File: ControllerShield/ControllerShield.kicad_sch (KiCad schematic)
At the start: 25 parts, among them J1 Power, J2 Digital/PWM, J3 Analog, J4 Digital/PWM, J5 Conn_02x05_Odd_Even, J6 Debug Point, SW1 Small Switch TH, U1 COM-09032, U2 LIS3DHTR, U3 TLV75533PDBV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

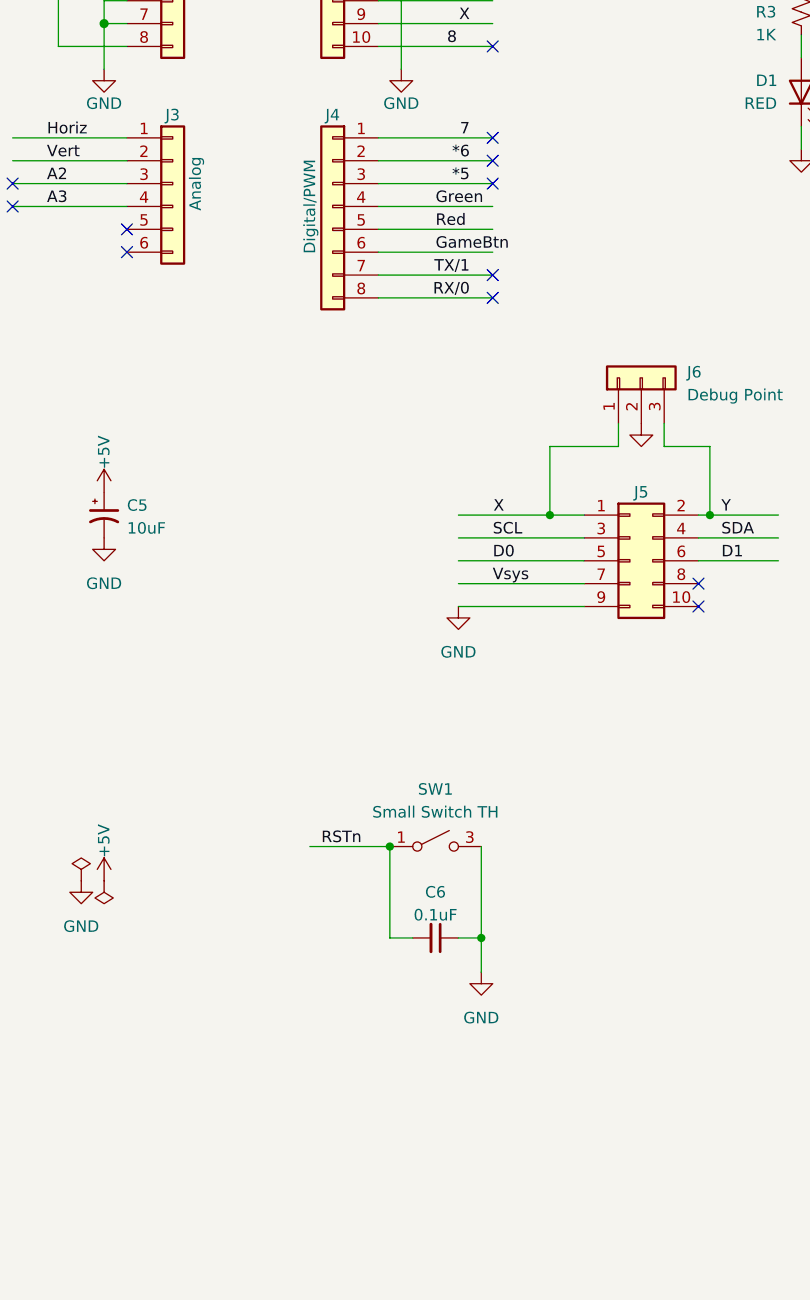
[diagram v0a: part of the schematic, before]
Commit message: Add a second switch to the controller board.
Generate V0.9 gerbers with QRCode.
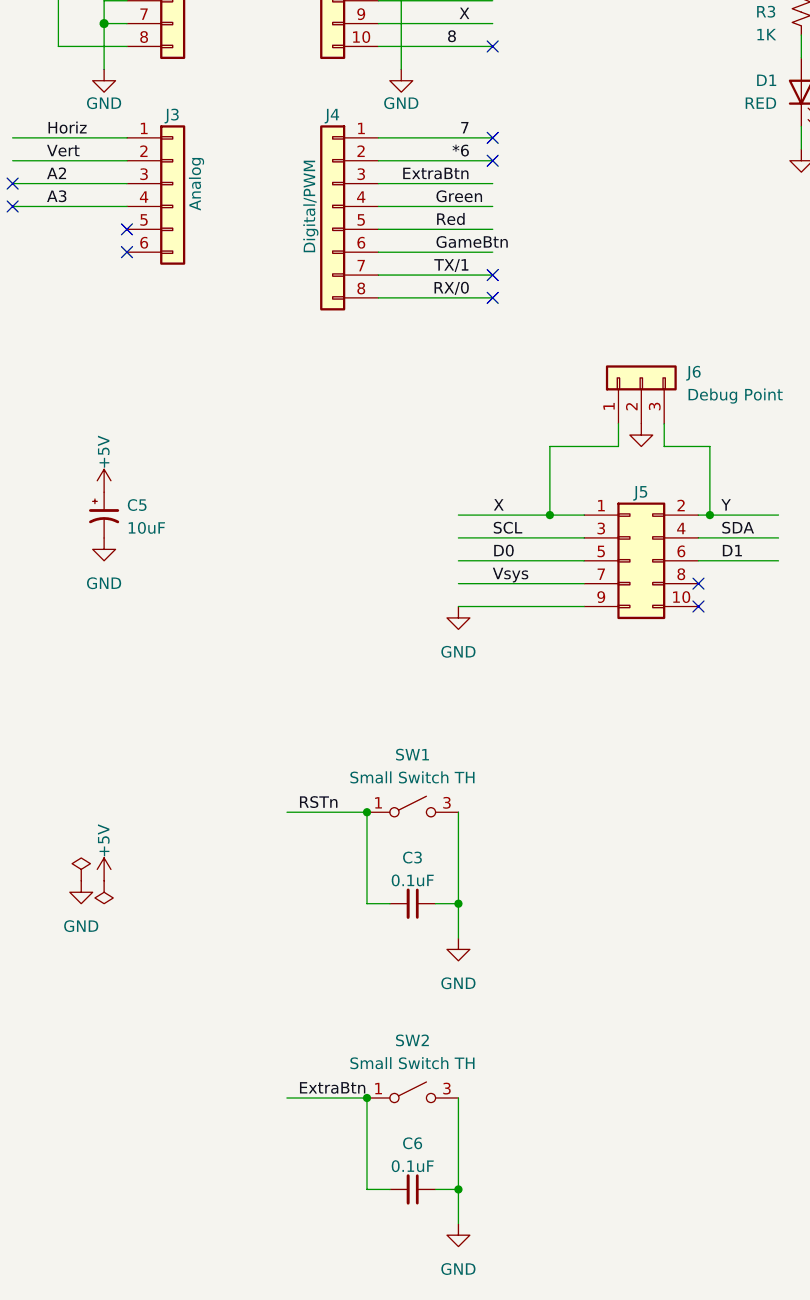
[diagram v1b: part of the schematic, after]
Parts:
- added C3: 0.1uF, Capacitor_SMD:C_0603_1608Metric, symbol Device:C_Small
- added SW2: Small Switch TH, Footprints:SW4_1825910-B_TEC, symbol Local:Small Switch TH
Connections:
- net GND: now also C3.1, SW2.3 (B), SW2.4 (B)
- net RSTn: now also C3.2; no longer C6.2
- net *5 renamed ExtraBtn
- net ExtraBtn: now also C6.2, SW2.1 (A), SW2.2 (A)
- no-connect marks 22 -> 21

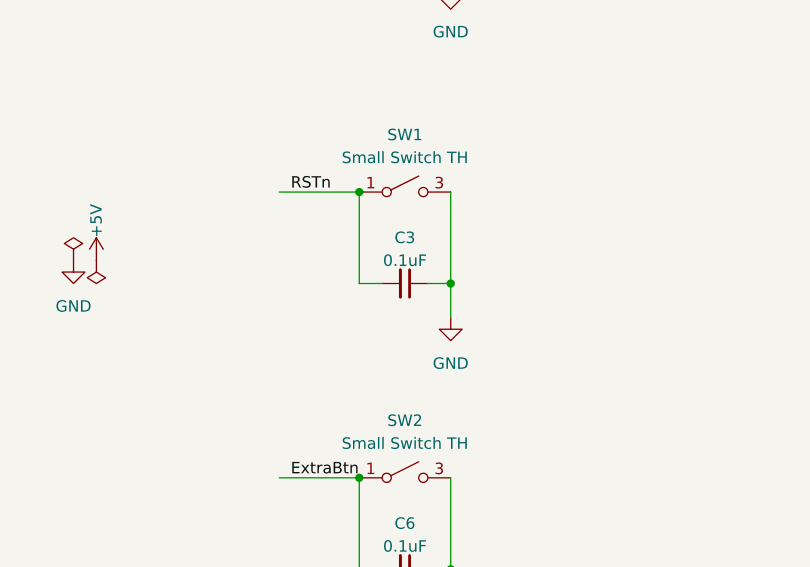
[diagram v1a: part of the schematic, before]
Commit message: add vendor id for level shifter
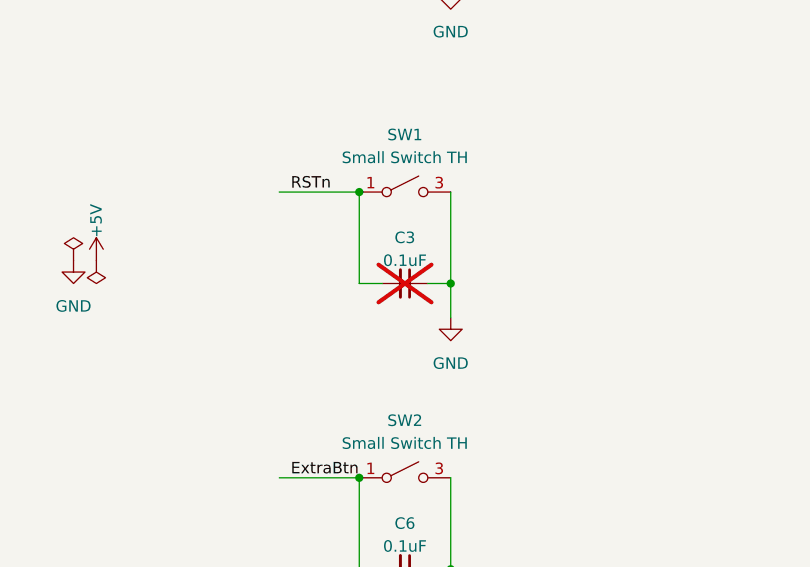
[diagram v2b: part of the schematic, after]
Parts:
- C3: now not fitted
- U4: DigiKey (none) -> 296-18509-2-ND; Vendor (none) -> 296-18509-2-ND
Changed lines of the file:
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@@
   )
   (symbol (lib_id "Device:C_Small") (at 66.04 144.78 270) (unit 1)
-    (in_bom yes) (on_board yes) (dnp no) (fields_autoplaced)
+    (in_bom yes) (on_board yes) (dnp yes) (fields_autoplaced)
     (property "Reference" "C3" (at 66.0336 139.7 90)
       (effects (font (size 1.27 1.27)))
@@
       (effects (font (size 1.27 1.27)) hide)
     )
+    (property "DigiKey" "296-18509-2-ND" (at 175.26 130.81 0)
+      (effects (font (size 1.27 1.27)) hide)
+    )
+    (property "Vendor" "296-18509-2-ND" (at 175.26 130.81 0)
+      (effects (font (size 1.27 1.27)) hide)
+    )

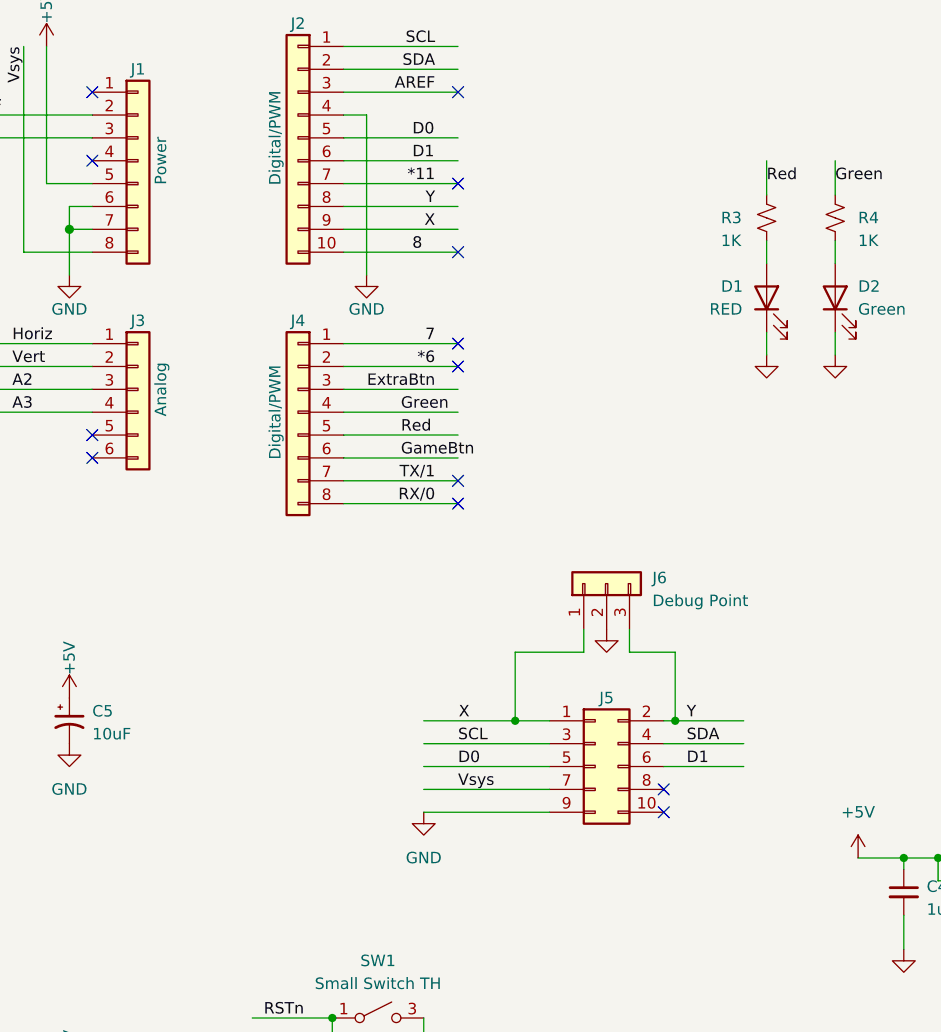
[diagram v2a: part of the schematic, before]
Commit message: Update controller shield to match the new driver.
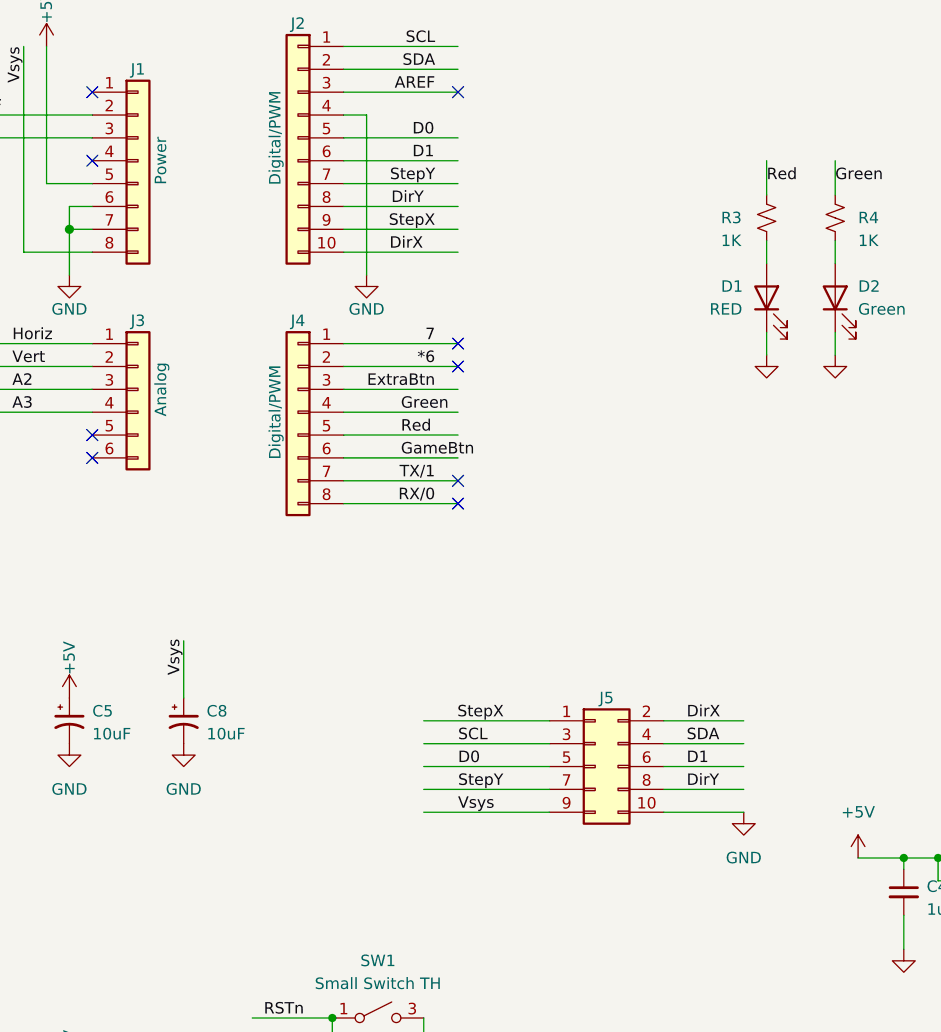
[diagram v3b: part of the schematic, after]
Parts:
- removed J6: Debug Point, Connector_PinHeader_2.54mm:PinHeader_1x03_P2.54mm_Vertical, symbol Connector_Generic:Conn_01x03
- added C8: 10uF, Capacitor_THT:CP_Radial_D6.3mm_P2.50mm, symbol Device:C_Polarized_Small_US
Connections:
- net GND: now also J5.10 (Pin_10), C8.2; no longer J5.9 (Pin_9)
- net Vsys: now also J5.9 (Pin_9), C8.1; no longer J5.7 (Pin_7)
- net DirY: now reaches J5.8 (Pin_8)
- net DirY: now also J2.8 (Pin_8)
- net *11 renamed StepY
- net StepY: now also J5.7 (Pin_7)
- net 8 renamed DirX
- net DirX: now also J5.2 (Pin_2)
- net X renamed StepX
- removed net Y: J2.8 (Pin_8), J5.2 (Pin_2)
- no-connect marks 21 -> 17
